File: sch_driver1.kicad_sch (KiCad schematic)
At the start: 20 parts, among them Q1 PSMN4R0-30YLDX, U1 ADA4099-2xR, U11 TS5A3159ADCK, U21 OPA365AIDBV, U3 ADA4099-1

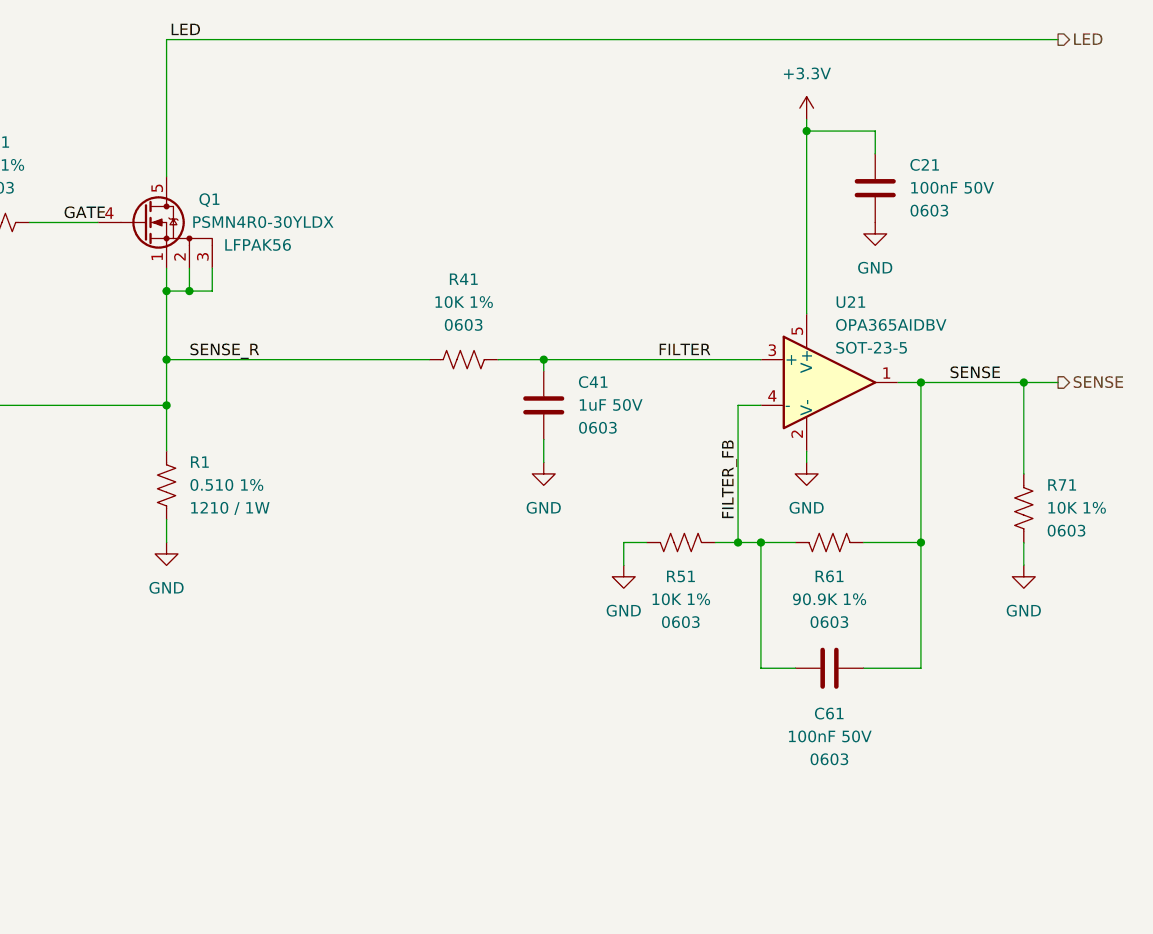
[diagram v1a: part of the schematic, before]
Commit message: Initial placement on 45 x 30 mm outline. Dropped sense apms. Switch to two 2x6 connectors.
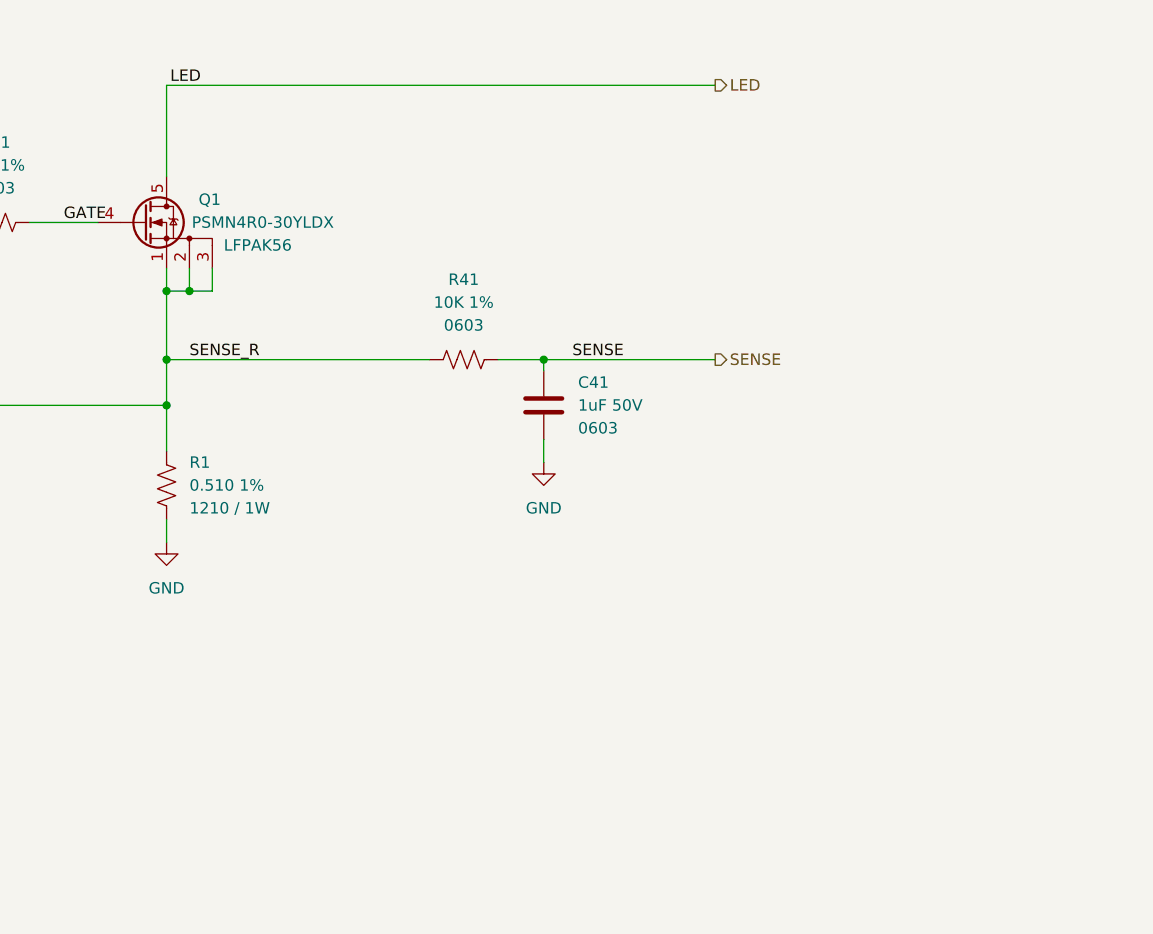
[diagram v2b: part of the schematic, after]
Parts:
- removed C21, C61: 100nF 50V, $Local:C_0603_1608Metric, symbol $Local:C_0603_100NF_50V
- removed R51, R71: 10K 1%, $Local:R_0603_1608Metric, symbol $Local:R_0603_10K
- removed R61: 90.9K 1%, $Local:R_0603_1608Metric, symbol $Local:R_0603_10K
- removed U21: OPA365AIDBV, $Local:SOT-23-5, symbol $Local:OPA365AIDBV
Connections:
- net FILTER is gone; now on net SENSE: C41.1, R41.1
